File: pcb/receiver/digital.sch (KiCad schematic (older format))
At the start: 59 parts, among them J301 UART, J302 STM32_SWD, J303 AVR_DEBUG, J304 USB_B_Micro, U301 ATTINY412-SSNR, U302 STM32F070F6P6, U303 MAX11666AUB+T, U304 L78L33ABUTR, Y301 ABM3B-8.000MHZ-10-1UT

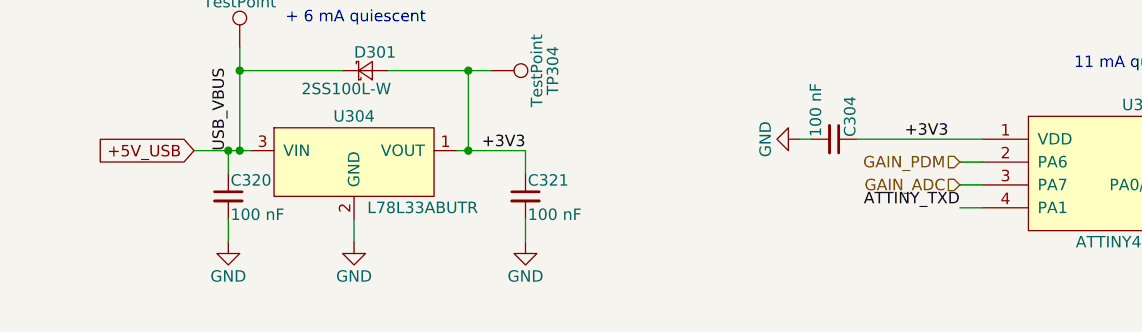
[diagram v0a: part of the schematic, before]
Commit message: Note missing components
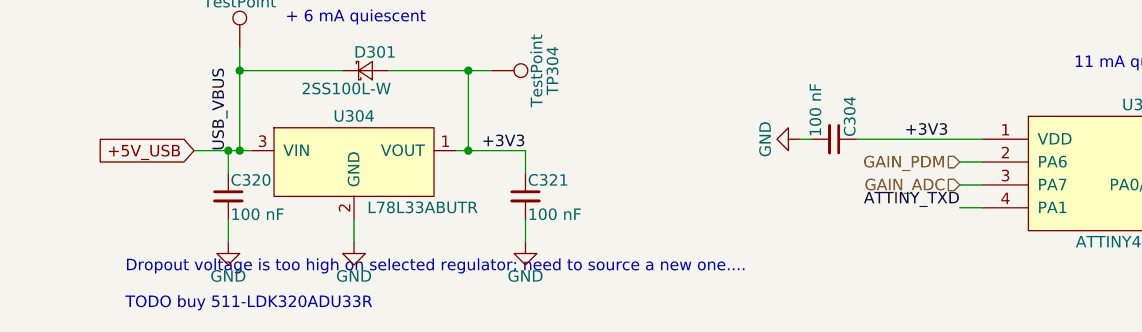
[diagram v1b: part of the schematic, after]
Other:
- note added: "Dropout voltage is too high on selected regulator; need to source a new one....\n\nTODO buy 511-LDK320ADU33R"
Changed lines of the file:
@@
 	2100 3800 2100 3550
 Connection ~ 2100 3550
+Text Notes 1100 6450 0    50   ~ 0
+Dropout voltage is too high on selected regulator; need to source a new one....\n\nTODO buy 511-LDK320ADU33R
 $EndSCHEMATC

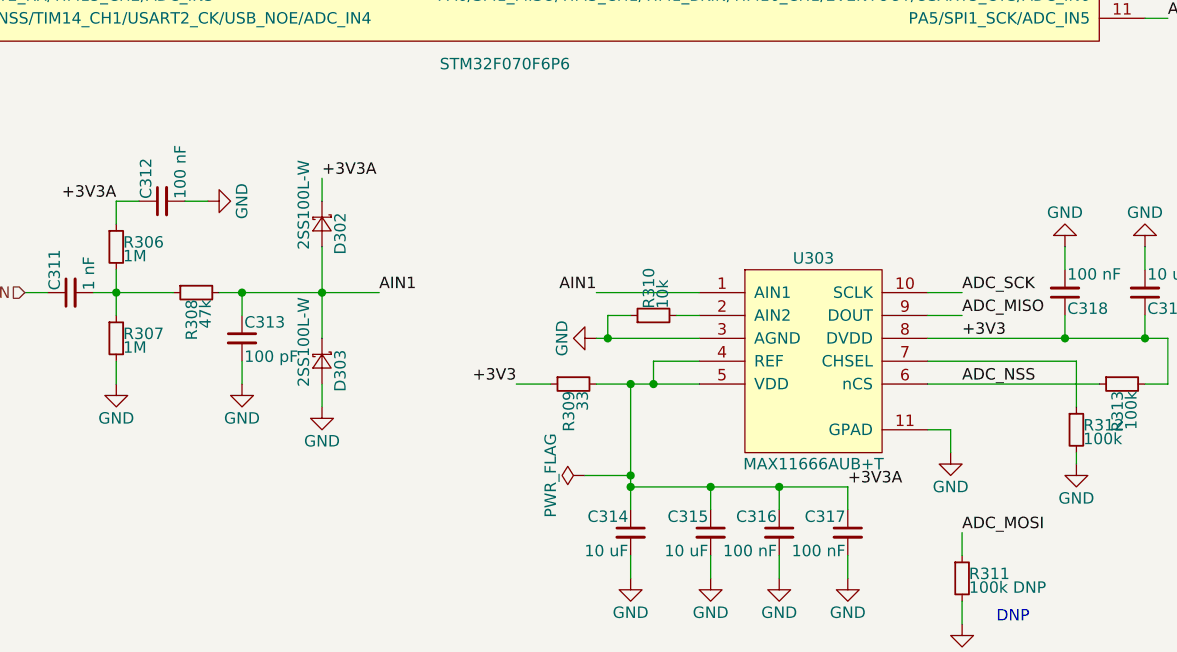
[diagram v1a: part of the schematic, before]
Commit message: Add in TODOs for a lot of small mistakes
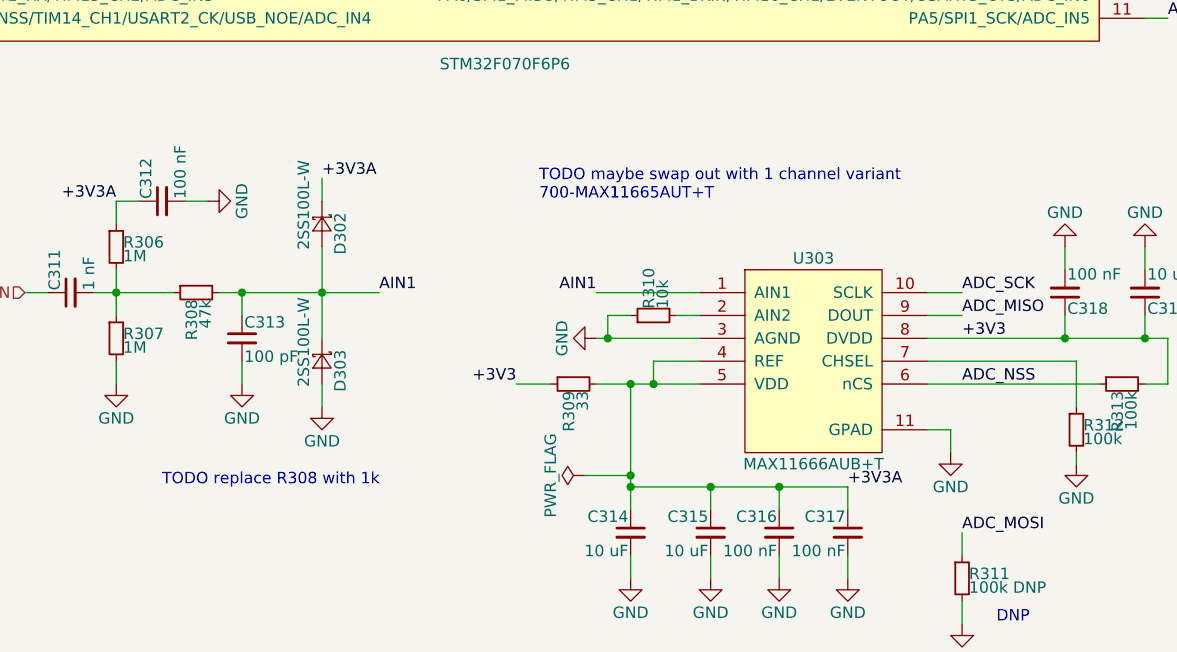
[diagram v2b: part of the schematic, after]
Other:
- note added: "TODO maybe swap out with 1 channel variant\n700-MAX11665AUT+T"
- note added: "TODO replace R308 with 1k"
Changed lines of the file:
@@
 Text Notes 1100 6450 0    50   ~ 0
 Dropout voltage is too high on selected regulator; need to source a new one....\n\nTODO buy 511-LDK320ADU33R
+Text Notes 5700 2900 0    50   ~ 0
+TODO maybe swap out with 1 channel variant\n700-MAX11665AUT+T
+Text Notes 4050 4150 0    50   ~ 0
+TODO replace R308 with 1k
 $EndSCHEMATC

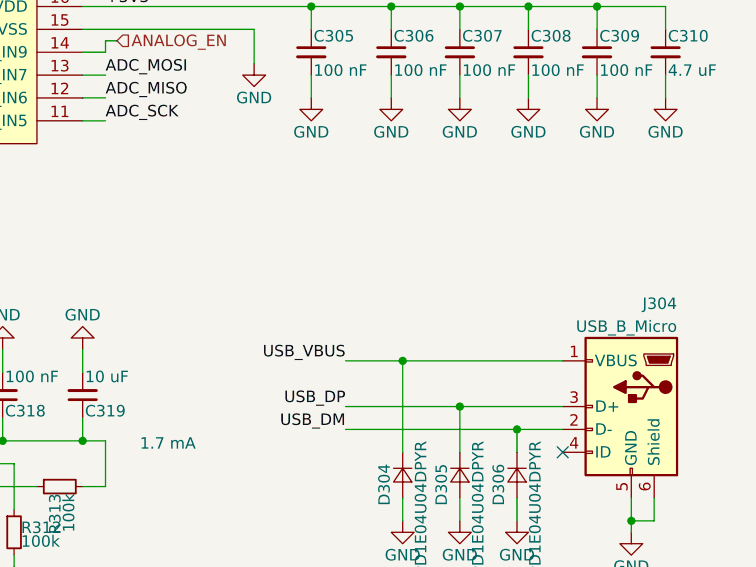
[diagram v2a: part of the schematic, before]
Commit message: Add note about ESD diodes
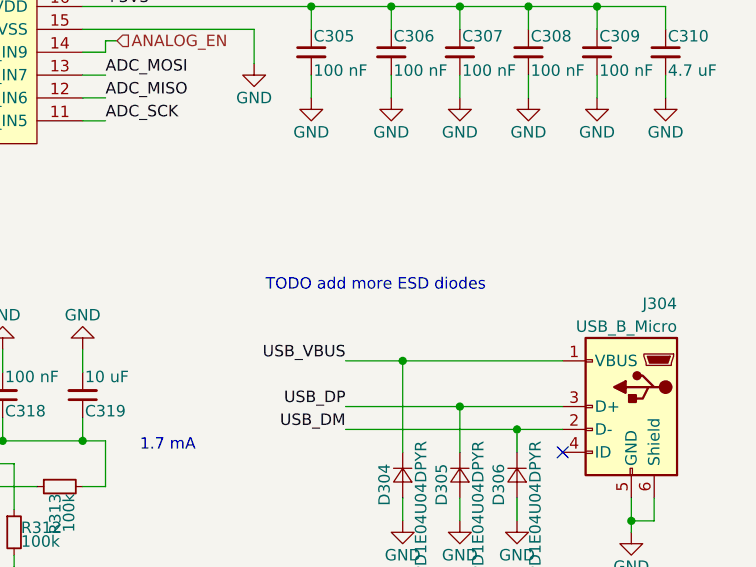
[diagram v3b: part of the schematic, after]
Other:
- note added: "TODO add more ESD diodes"
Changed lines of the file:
@@
 Text Notes 4050 4150 0    50   ~ 0
 TODO replace R308 with 1k
+Text Notes 9150 2850 0    50   ~ 0
+TODO add more ESD diodes
 $EndSCHEMATC
